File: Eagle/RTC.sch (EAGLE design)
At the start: 32 parts, among them IC1 MEGA32-P, Q1 BC817-16LT1SMD, Q2 BC817-16LT1SMD, Q3 BC817-16LT1SMD, Q4 BC817-16LT1SMD, Q5 BC817-16LT1SMD, Q6 BC817-16LT1SMD

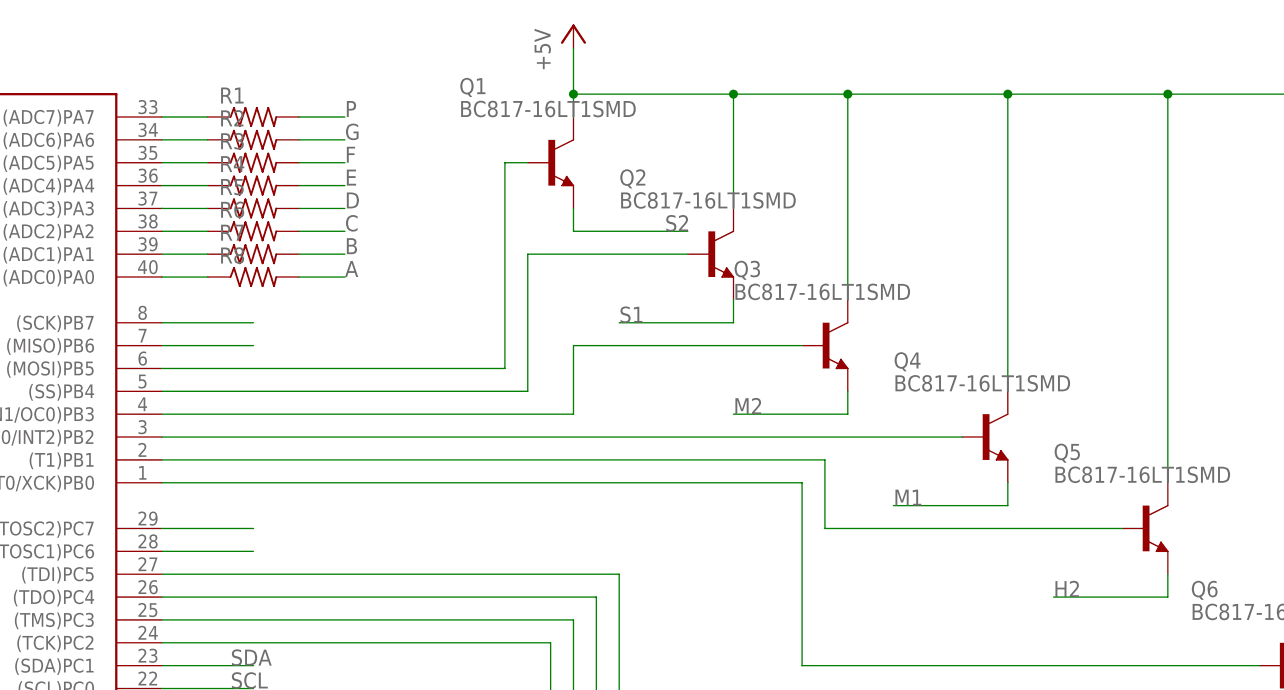
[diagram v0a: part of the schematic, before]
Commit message: Added Base Resistors.
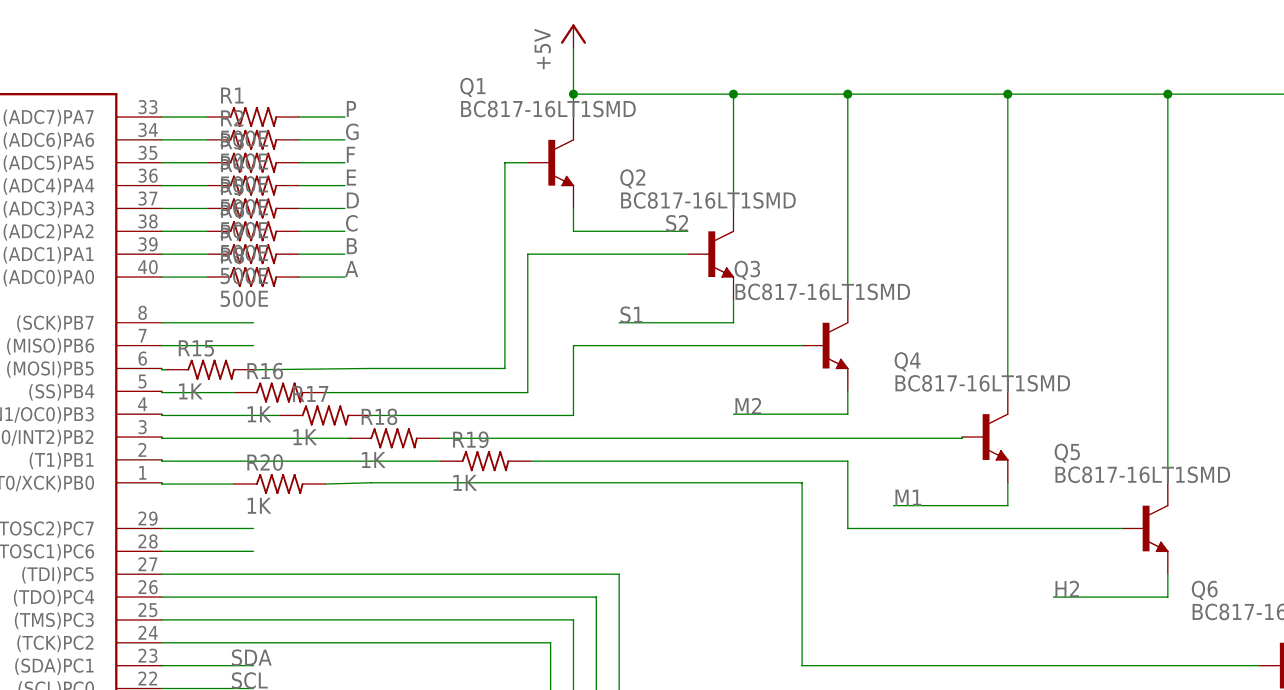
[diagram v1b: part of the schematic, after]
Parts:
- added R15, R16, R17, R18, R19, R20: 1K, rcl:R-US_M1206
- R1, R2, R3, R4, R5, R6, R7, R8: value (none) -> 500E
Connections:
- removed net N$147: IC1.(AIN0/INT2)PB2, Q4.B
- new net N$10: IC1.(T0/XCK)PB0, R20.1
- new net N$11: Q4.B, R18.2
- new net N$5: IC1.(MOSI)PB5, R15.1
- new net N$6: IC1.(SS)PB4, R16.1
- new net N$7: IC1.(AIN1/OC0)PB3, R17.1
- new net N$8: IC1.(AIN0/INT2)PB2, R18.1
- new net N$9: IC1.(T1)PB1, R19.1
- net N$128: now also R15.2; no longer IC1.(MOSI)PB5
- net N$129: now also R16.2; no longer IC1.(SS)PB4
- net N$130: now also R17.2; no longer IC1.(AIN1/OC0)PB3
- net N$148: now also R19.2; no longer IC1.(T1)PB1
- net N$149: now also R20.2; no longer IC1.(T0/XCK)PB0
